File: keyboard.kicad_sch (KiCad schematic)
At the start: 39 parts, among them U1 Elite-C-castellated-24pin

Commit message: RP2040 rework
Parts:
- removed U1: Elite-C-castellated-24pin, Keebio-Parts:Elite-C-castellated-24pin, symbol promicro:ProMicro
- added C1, C3, C4: 1u, symbol Device:C
- added C2: 30p, symbol Device:C
- added J1: USB4085-GF-A_REVA4, LordsBoard:GCT_USB4085-GF-A_REVA4, symbol USB_C_THT:USB4085-GF-A_REVA4
- added R1, R2: 5k1, symbol Device:R_Small_US
- added R3, R4: 27, symbol Device:R_Small_US
- added U1: XC6206P332MR, Package_TO_SOT_SMD:SOT-23, symbol Regulator_Linear:XC6206PxxxMR
- added U2: SRV05-4, Package_TO_SOT_SMD:SOT-23-6, symbol Power_Protection:SRV05-4
- added U3: RP2040, MCU_RaspberryPi_and_Boards:RP2040-QFN-56, symbol MCU_RaspberryPi_and_Boards:RP2040
- added Y1: Crystal, Crystal:Crystal_SMD_0603-2Pin_6.0x3.5mm, symbol Device:Crystal
- renumbered D_SPACE4 to D_SPACE1, D_SPACE7 to D_SPACE10, D_SPACE15 to D_SPACE11, D_SPACE19 to D_SPACE12, D_SPACE8 to D_SPACE13, D_SPACE12 to D_SPACE14, D_SPACE16 to D_SPACE15, D_SPACE17 to D_SPACE16, D_SPACE18 to D_SPACE17, D_SPACE9 to D_SPACE18, D_SPACE10 to D_SPACE19, D_SPACE5 to D_SPACE2, D_SPACE11 to D_SPACE3, D_SPACE1 to D_SPACE4, D_SPACE13 to D_SPACE5, D_SPACE2 to D_SPACE6, D_SPACE6 to D_SPACE7, D_SPACE14 to D_SPACE8, D_SPACE3 to D_SPACE9, K_SPACE4 to K_SPACE1, K_SPACE7 to K_SPACE10, K_SPACE15 to K_SPACE11, K_SPACE19 to K_SPACE12, K_SPACE8 to K_SPACE13, K_SPACE12 to K_SPACE14, K_SPACE16 to K_SPACE15, K_SPACE17 to K_SPACE16, K_SPACE18 to K_SPACE17, K_SPACE9 to K_SPACE18, K_SPACE10 to K_SPACE19, K_SPACE5 to K_SPACE2, K_SPACE11 to K_SPACE3, K_SPACE1 to K_SPACE4, K_SPACE13 to K_SPACE5, K_SPACE2 to K_SPACE6, K_SPACE6 to K_SPACE7, K_SPACE14 to K_SPACE8, K_SPACE3 to K_SPACE9
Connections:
- net col0: now also U3.8 (GPIO6)
- net col1: now also U3.9 (GPIO7)
- net col2: now also U3.11 (GPIO8)
- net col3: now also U3.12 (GPIO9)
- net col4: now also U3.13 (GPIO10)
- net col5: now also U3.14 (GPIO11)
- net col6: now also U3.15 (GPIO12)
- net row0: now also U3.2 (GPIO0)
- net row1: now also U3.3 (GPIO1)
- net row2: now also U3.4 (GPIO2)
- net row3: now also U3.5 (GPIO3)
- net row4: now also U3.6 (GPIO4)
- net row5: now also U3.7 (GPIO5)
- new net: J1.B5 (CC2), R1.1
- new net: R3.1, U3.47 (USB_DP)
- new net: J1.A5 (CC1), R2.1
- new net: U3.23 (DVDD), U3.45 (VREG_VOUT), U3.50 (DVDD)
- new net: R4.1, U3.46 (USB_DM)
- new net +3V3: C4.1, U1.2 (VO), U3.1 (IOVDD), U3.10 (IOVDD), U3.22 (IOVDD), U3.33 (IOVDD), U3.42 (IOVDD), U3.43 (ADC_AVDD), U3.44 (VREG_IN), U3.48 (USB_VDD), U3.49 (IOVDD)
- new net +5V: C1.1, J1.A4 (VBUS), J1.A9 (VBUS), J1.B4 (VBUS), J1.B9 (VBUS), U1.3 (VI), U2.5 (VP)
- new net CLK_IN: C2.2, U3.20 (XIN), Y1.1
- new net CLK_OUT: C3.1, U3.21 (XOUT), Y1.2
- new net DN1: J1.A7 (DN1), J1.B7 (DN2), R4.2, U2.4 (IO3), U2.6 (IO4)
- new net DP1: J1.A6 (DP1), J1.B6 (DP2), R3.2, U2.1 (IO1), U2.3 (IO2)
- new net GND: C1.2, C2.1, C3.2, C4.2, J1.A1 (GND), J1.A12 (GND), J1.B1 (GND), J1.B12 (GND), J1.P1 (SHELL), J1.P2 (SHELL), J1.P3 (SHELL), J1.P4 (SHELL), R1.2, R2.2, U1.1 (GND), U2.2 (VN), U3.19 (TESTEN), U3.57 (GND)
- new net RST: U3.26 (RUN)
- no-connect marks 11 -> 14

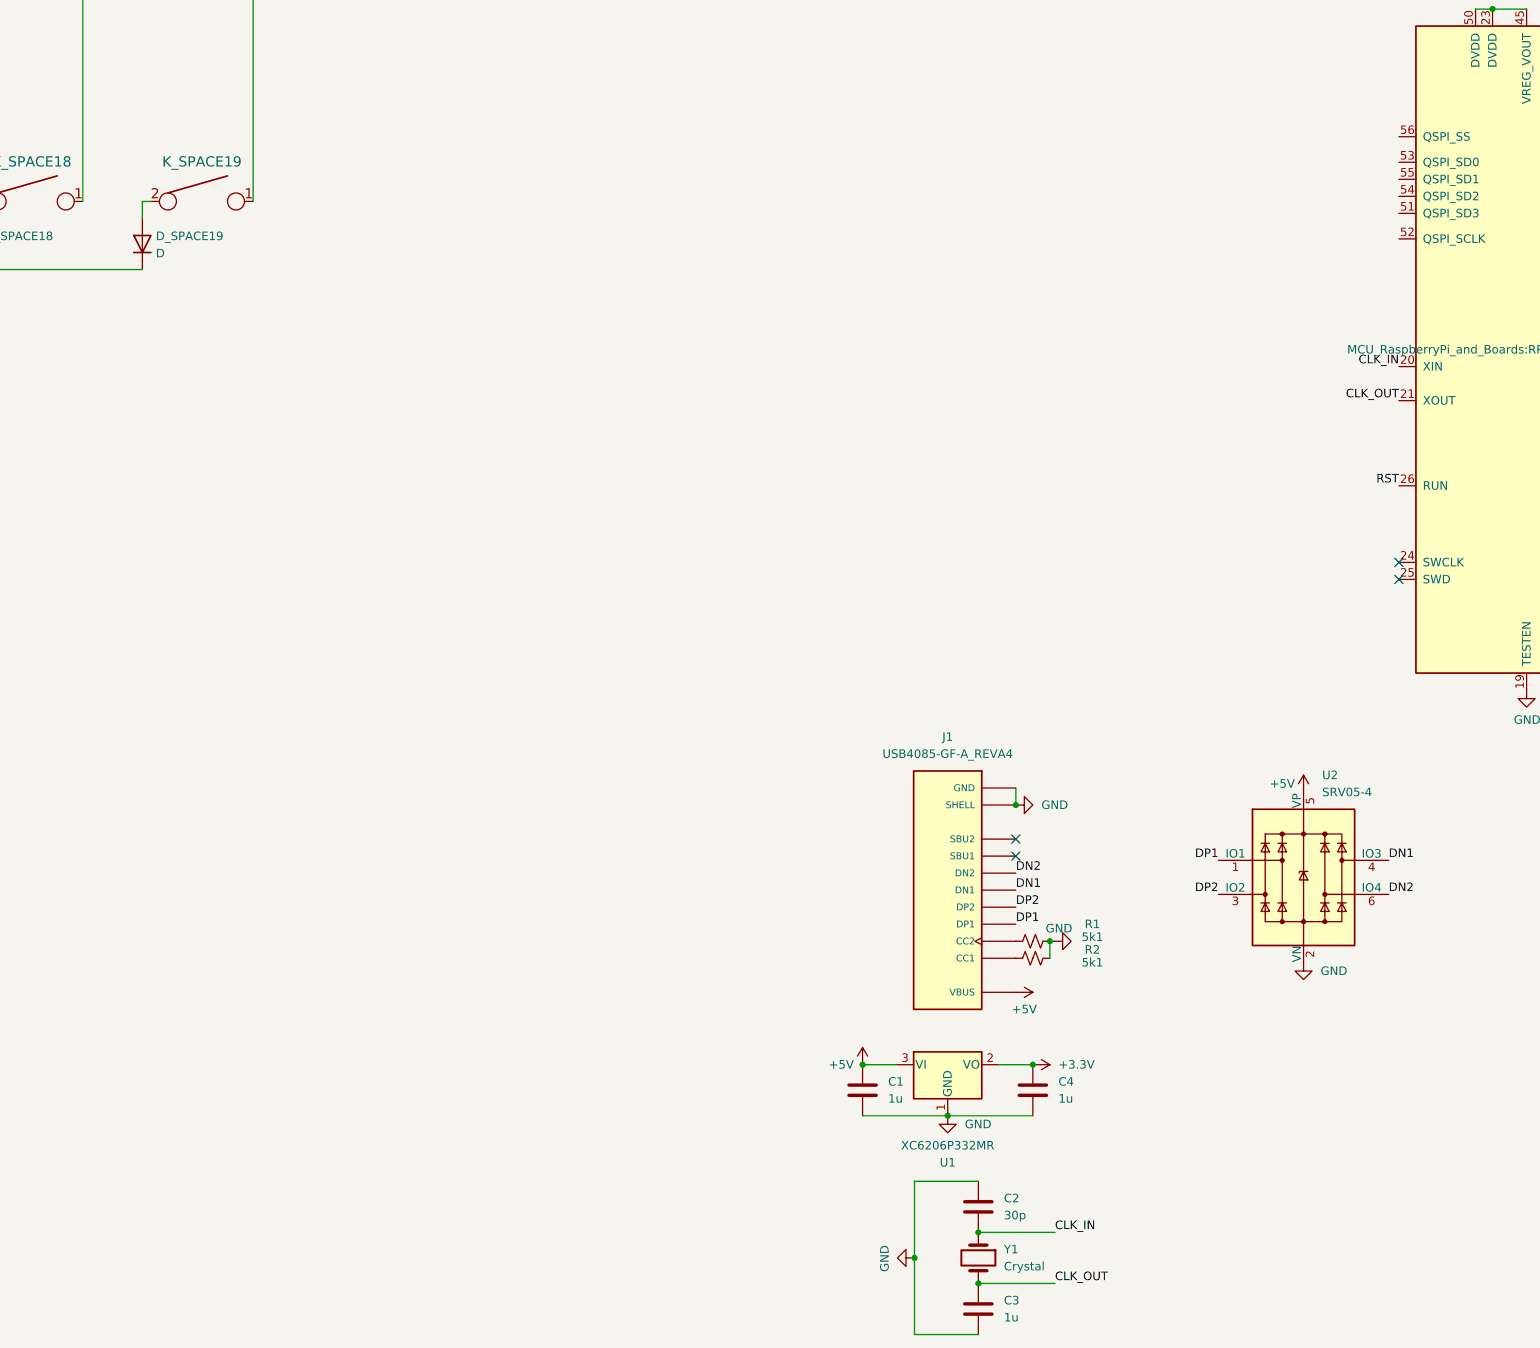
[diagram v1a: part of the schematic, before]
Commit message: Changes to keyboard schematic--added QSPI flash.  TODO: add decoupling caps.
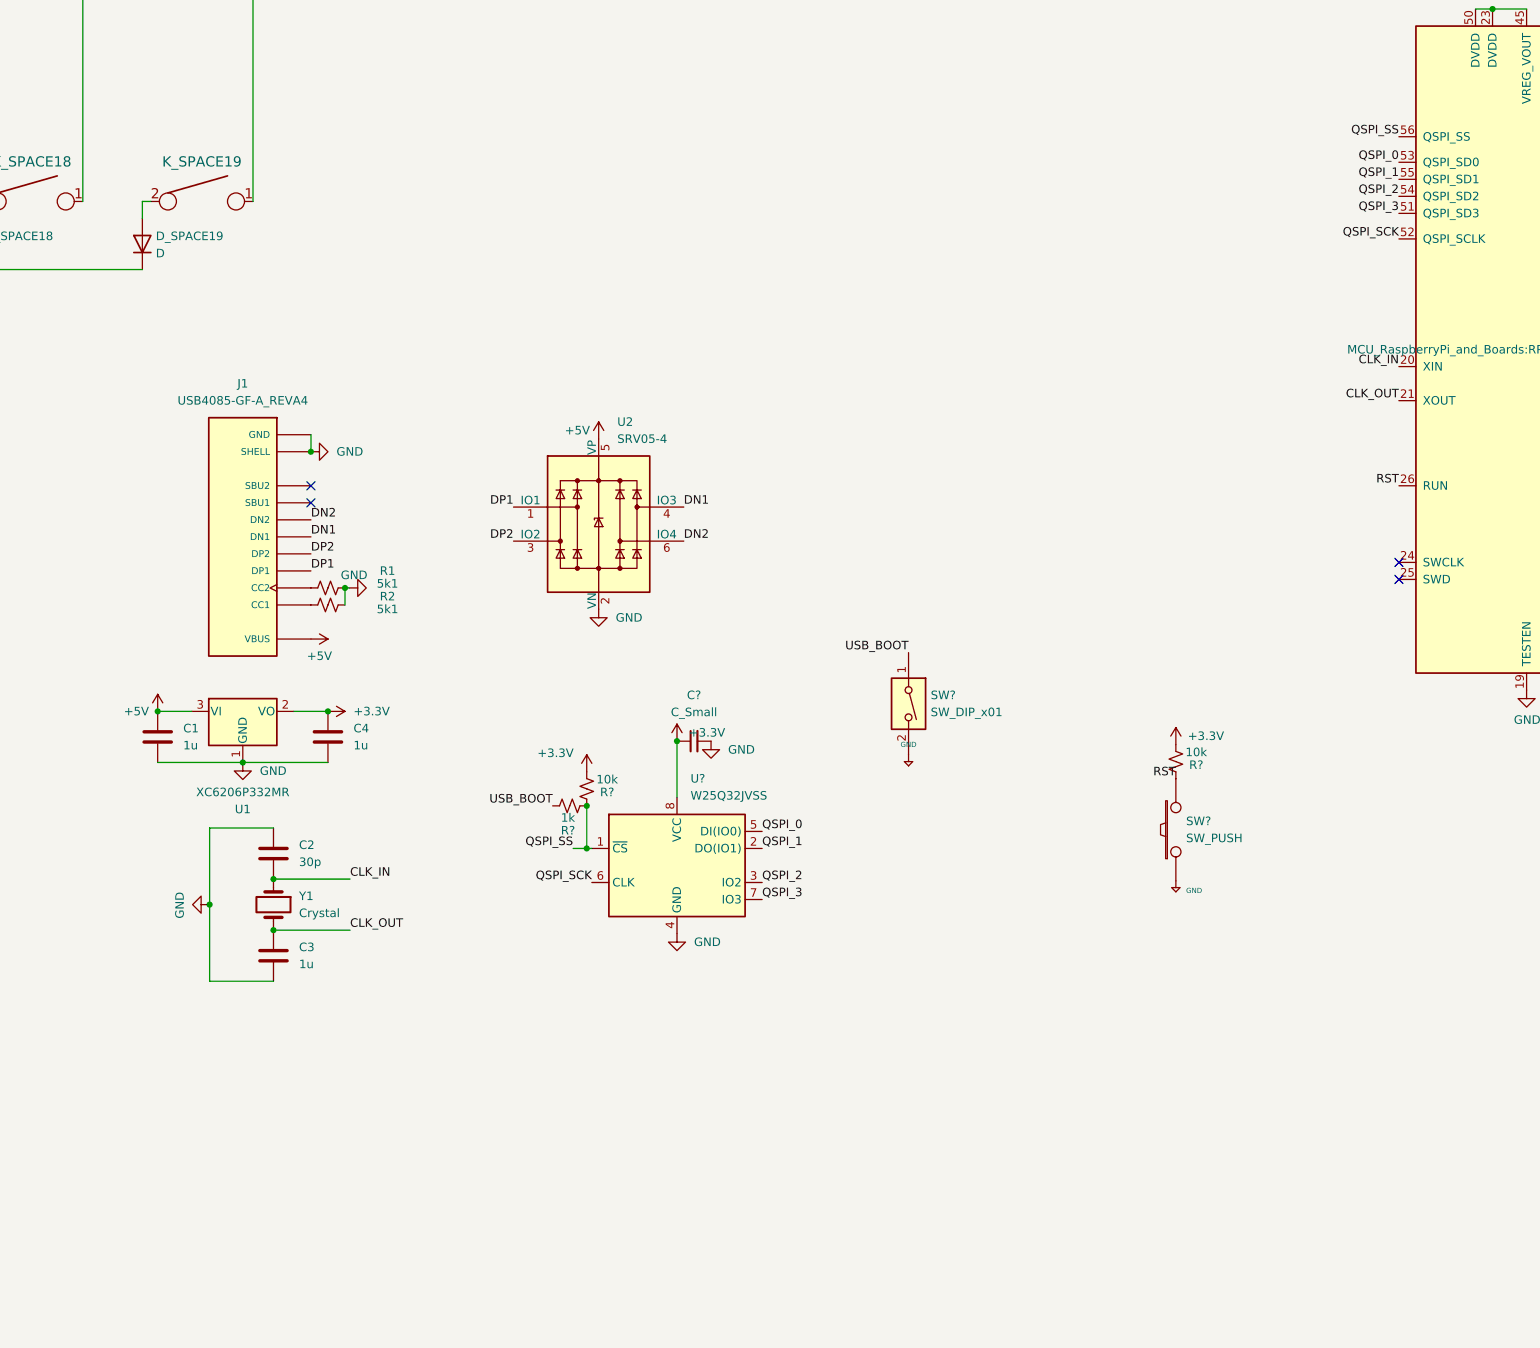
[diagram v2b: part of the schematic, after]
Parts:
- added C?: C_Small, symbol Device:C_Small
- added R? (x2): 10k, symbol Device:R_Small_US
- added R?: 1k, symbol Device:R_Small_US
- added SW?: SW_PUSH, symbol keyboard_parts:SW_PUSH
- added SW?: SW_DIP_x01, symbol Switch:SW_DIP_x01
- added U?: W25Q32JVSS, Package_SO:SOIC-8_5.23x5.23mm_P1.27mm, symbol Memory_Flash:W25Q32JVSS
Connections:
- net +3V3: now also C?.1, R?.2, R?.2, U?.8 (VCC)
- net +5V: now also SW?.1, SW?.2
- net GND: now also C?.2, U?.4 (GND)
- net RST: now also R?.1, SW?.2
- net QSPI_3: now reaches U3.51 (QSPI_SD3)
- net QSPI_3: now also U?.7 (IO3)
- net QSPI_SCK: now reaches U3.52 (QSPI_SCLK)
- net QSPI_SCK: now also U?.6 (CLK)
- net QSPI_0: now reaches U3.53 (QSPI_SD0)
- net QSPI_0: now also U?.5 (DI(IO0))
- net QSPI_2: now reaches U3.54 (QSPI_SD2)
- net QSPI_2: now also U?.3 (IO2)
- net QSPI_1: now reaches U3.55 (QSPI_SD1)
- net QSPI_1: now also U?.2 (DO(IO1))
- net QSPI_SS: now reaches U3.56 (QSPI_SS)
- net QSPI_SS: now also R?.1, R?.1, U?.1 (~{CS})
- new net USB_BOOT: R?.2, SW?.1
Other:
- moved on the sheet: C1, C2, C3, C4, J1, R1, R2, U1, U2, Y1
